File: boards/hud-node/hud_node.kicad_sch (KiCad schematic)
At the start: 3 parts

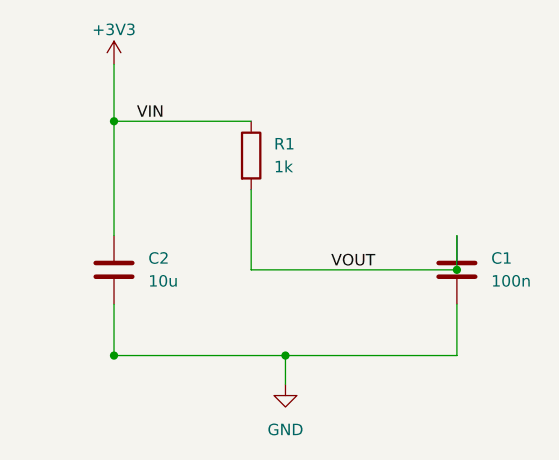
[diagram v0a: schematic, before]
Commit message: Implement all CI jobs and auto-BOM generation
- generate_bom.py: real implementation that parses .kicad_sch S-expressions
  directly (stdlib only) and writes bom/consolidated-bom.csv, one line item
  per part per board; handles DNP exclusion, multi-unit symbols, hierarchical
  sheet instances, and MPN/Manufacturer properties; --check mode for CI
- ci.yml: replace all placeholder jobs with real ones
  - erc-drc: kicad-cli sch erc / pcb drc per board in kicad/kicad:9.0,
    reports uploaded as artifacts
  - render-artifacts: schematic PDFs + front/back PCB layer SVGs
  - bom: --check on PRs (fail if committed CSV is stale) with BOM diff vs
    base in the job summary; auto-commit regenerated CSV on pushes to main
  - interactive-html-bom: InteractiveHtmlBom v2.11.2 per board
  - harness-render: WireViz -> SVG for harness YAML (no-op until sources exist)
  - triggers expanded to libraries/bom/harness/workflow paths + dispatch
- hud-node stub board: fix so ERC/DRC actually pass (verified locally with
  kicad-cli 9.0.3): add PWR_FLAGs for the undriven power nets, fix R1 pad 1
  net (VIN -> +3V3, matching schematic net resolution), un-rotate C1/C2 so
  pads sit on the trace grid, reroute all three nets without crossings
- README: pin team KiCad version to 9.0 (matches CI image), document the
  BOM regeneration workflow

Co-Authored-By: Claude Fable 5 <noreply@anthropic.com>
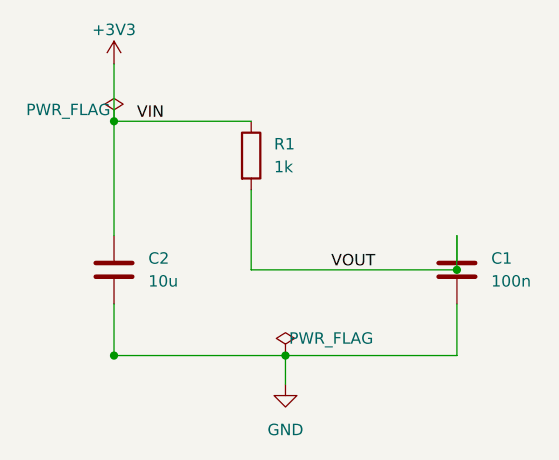
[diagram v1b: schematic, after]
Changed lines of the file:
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@@
+		)
+	)
+	(symbol
+		(lib_id "power:PWR_FLAG")
+		(at 111.76 72.39 0)
+		(unit 1)
+		(exclude_from_sim no)
+		(in_bom yes)
+		(on_board yes)
+		(dnp no)
+		(property "Reference" "#FLG01" (at 111.76 70.485 0) (effects (font (size 1.27 1.27)) (hide yes)))
+		(property "Value" "PWR_FLAG" (at 106.68 71.12 0) (effects (font (size 1.27 1.27))))
+		(property "Footprint" "" (at 111.76 72.39 0) (effects (font (size 1.27 1.27)) (hide yes)))
+		(property "Datasheet" "~" (at 111.76 72.39 0) (effects (font (size 1.27 1.27)) (hide yes)))
+		(property "Description" "Special symbol for telling ERC where power comes from" (at 111.76 72.39 0) (effects (font (size 1.27 1.27)) (hide yes)))
+		(pin "1")
+		(instances
+			(project "hud_node"
+				(path "/0f1e2d3c-4b5a-6978-8899-aabbccddeeff"
+					(reference "#FLG01") (unit 1)
+				)
+			)
+		)
+	)
+	(symbol
+		(lib_id "power:PWR_FLAG")
+		(at 130.81 98.42 0)
+		(unit 1)
+		(exclude_from_sim no)
+		(in_bom yes)
+		(on_board yes)
+		(dnp no)
+		(property "Reference" "#FLG02" (at 130.81 96.515 0) (effects (font (size 1.27 1.27)) (hide yes)))
+		(property "Value" "PWR_FLAG" (at 135.89 96.52 0) (effects (font (size 1.27 1.27))))
+		(property "Footprint" "" (at 130.81 98.42 0) (effects (font (size 1.27 1.27)) (hide yes)))
+		(property "Datasheet" "~" (at 130.81 98.42 0) (effects (font (size 1.27 1.27)) (hide yes)))
+		(property "Description" "Special symbol for telling ERC where power comes from" (at 130.81 98.42 0) (effects (font (size 1.27 1.27)) (hide yes)))
+		(pin "1")
+		(instances
+			(project "hud_node"
+				(path "/0f1e2d3c-4b5a-6978-8899-aabbccddeeff"
+					(reference "#FLG02") (unit 1)
+				)
+			)
 		)
 	)
